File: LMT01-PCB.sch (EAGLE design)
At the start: 14 parts, among them IC3 PIC16F1826/27SO, IC4 MAX3467CPA, IC6 MCP23017SO

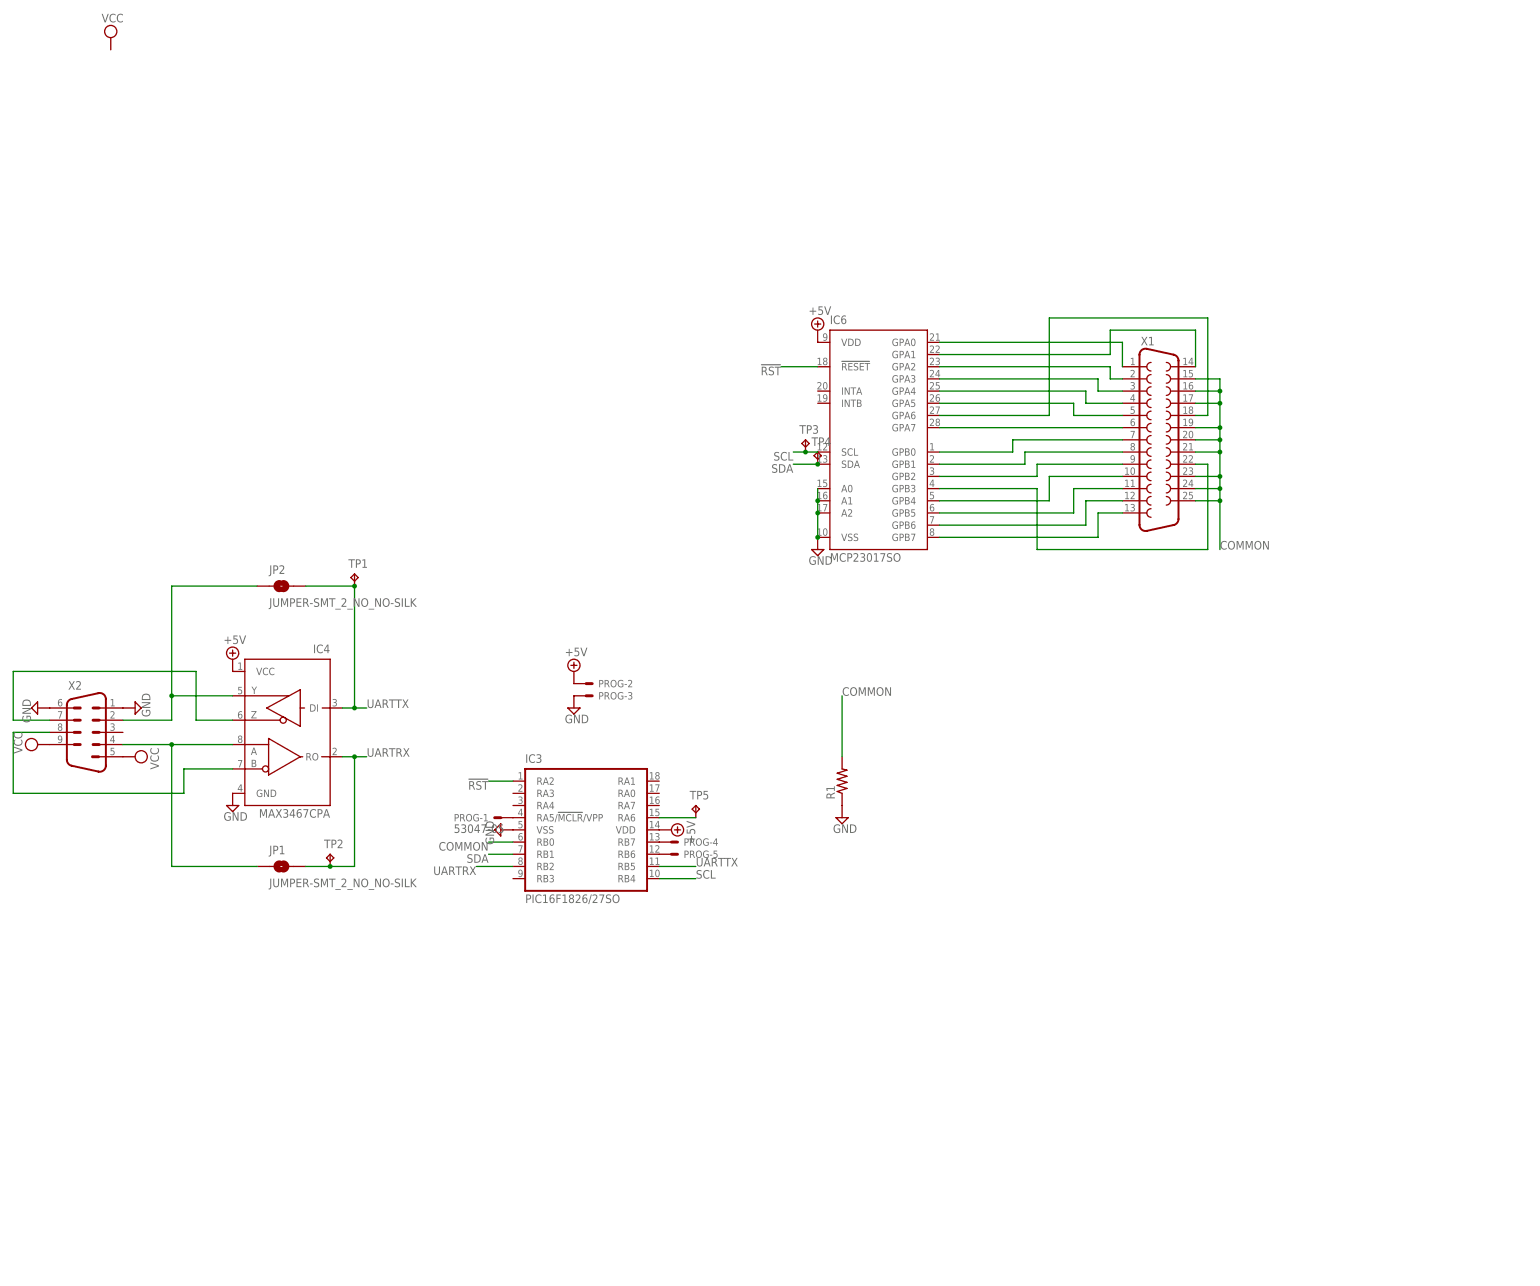
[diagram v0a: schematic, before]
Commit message: Switching to big PIC
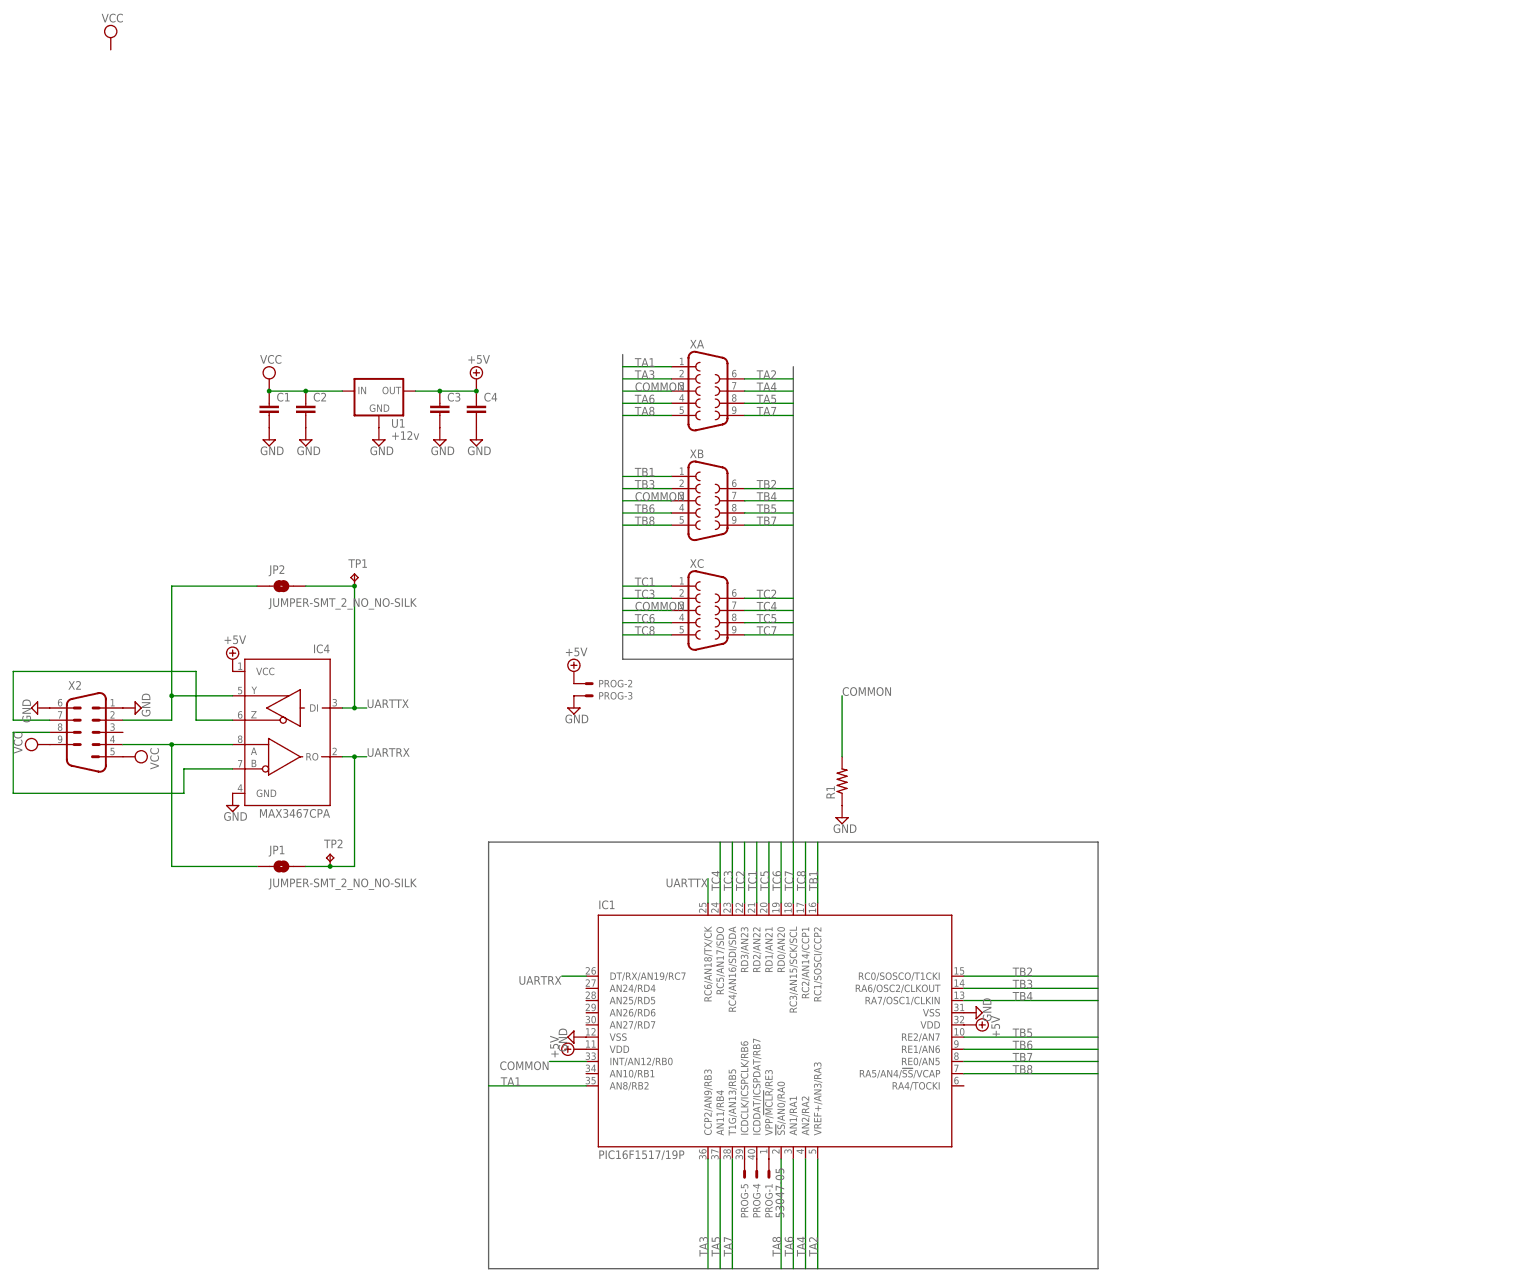
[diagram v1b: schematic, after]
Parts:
- removed IC3: PIC16F1826/27SO, microchip:PIC16F1826/27SO
- removed IC6: MCP23017SO, microchip:MCP23017SO
- removed TP3, TP4, TP5: TPB1,27, testpad:TPB1,27
- removed X1: (no value), con-subd:F25HP
- added C1, C2, C3, C4: (no value), resistor:C-EUC1206
- added IC1: PIC16F1517/19P, microchip:PIC16F1517/19P
- added U1: +12v, SparkFun-IC-Power:V_REG_78XX7812
- added XA, XB, XC: (no value), con-subd:F09HP
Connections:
- removed net !RST: IC3.RA2, IC6.!RESET
- removed net N$10: IC6.GPA5, X1.5
- removed net N$11: IC6.GPA6, X1.18
- removed net N$12: IC6.GPA7, X1.6
- removed net N$13: IC6.GPB0, X1.7
- removed net N$14: IC6.GPB1, X1.8
- removed net N$15: IC6.GPB2, X1.9
- removed net N$16: IC6.GPB3, X1.22
- removed net N$17: IC6.GPB4, X1.10
- removed net N$18: IC6.GPB5, X1.11
- removed net N$19: IC6.GPB6, X1.12
- removed net N$20: IC6.GPB7, X1.13
- removed net N$25: IC3.RB7, PROG-4.S
- removed net N$26: IC3.RB6, PROG-5.S
- removed net N$5: IC6.GPA0, X1.1
- removed net N$6: IC6.GPA1, X1.14
- removed net N$7: IC6.GPA2, X1.2
- removed net N$8: IC6.GPA3, X1.3
- removed net N$9: IC6.GPA4, X1.4
- removed net SCL: IC3.RB4, IC6.SCL, TP3.TP
- removed net SDA: IC3.RB1, IC6.SDA, TP4.TP
- new net N$2: IC1.ICDDAT/ICSPDAT/RB7, PROG-4.S
- new net TA1: IC1.AN8/RB2, XA.1
- new net TA2: IC1.VREF+/AN3/RA3, XA.6
- new net TA3: IC1.CCP2/AN9/RB3, XA.2
- new net TA4: IC1.AN2/RA2, XA.7
- new net TA5: IC1.AN11/RB4, XA.8
- new net TA6: IC1.AN1/RA1, XA.4
- new net TA7: IC1.T1G/AN13/RB5, XA.9
- new net TA8: IC1.!SS!/AN0/RA0, XA.5
- new net TB1: IC1.RC1/SOSCI/CCP2, XB.1
- new net TB2: IC1.RC0/SOSCO/T1CKI, XB.6
- new net TB3: IC1.RA6/OSC2/CLKOUT, XB.2
- new net TB4: IC1.RA7/OSC1/CLKIN, XB.7
- new net TB5: IC1.RE2/AN7, XB.8
- new net TB6: IC1.RE1/AN6, XB.4
- new net TB7: IC1.RE0/AN5, XB.9
- new net TB8: IC1.RA5/AN4/!SS!/VCAP, XB.5
- new net TC1: IC1.RD2/AN22, XC.1
- new net TC2: IC1.RD3/AN23, XC.6
- new net TC3: IC1.RC4/AN16/SDI/SDA, XC.2
- new net TC4: IC1.RC5/AN17/SDO, XC.7
- new net TC5: IC1.RD1/AN21, XC.8
- new net TC6: IC1.RD0/AN20, XC.4
- new net TC7: IC1.RC3/AN15/SCK/SCL, XC.9
- new net TC8: IC1.RC2/AN14/CCP1, XC.5
- net +5V: now also C3.1, C4.1, IC1.VDD, IC1.VDD@1, U1.OUT; no longer IC3.VDD, IC6.VDD
- net COMMON: now also IC1.INT/AN12/RB0, XA.3, XB.3, XC.3; no longer IC3.RB0, X1.15, X1.16, X1.17, X1.19, X1.20, X1.21, X1.23, X1.24, X1.25
- net GND: now also C1.2, C2.2, C3.2, C4.2, IC1.VSS, IC1.VSS@1, U1.GND; no longer IC3.VSS, IC6.A0, IC6.A1, IC6.A2, IC6.VSS
- net N$1: now also IC1.VPP/!MCLR!/RE3, PROG-1.S; no longer IC3.RA6, TP5.TP
- net N$3: now also IC1.ICDCLK/ICSPCLK/RB6, PROG-5.S; no longer IC3.RA5/!MCLR!/VPP, PROG-1.S
- net UARTRX: now also IC1.DT/RX/AN19/RC7; no longer IC3.RB2
- net UARTTX: now also IC1.RC6/AN18/TX/CK; no longer IC3.RB5
- net VCC: now also C1.1, C2.1, U1.IN
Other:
- moved on the sheet: PROG-1, PROG-4, PROG-5

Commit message: PIC18
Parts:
- added C5, C6: (no value), resistor:C-EUC1206
- added R2, R3: (no value), resistor:R-US_R1206
- IC1: value PIC16F1517/19P -> PIC18F47K40; device microchip:PIC16F1517/19P -> microchip:PIC18F47K40
- renumbered U1 to IC2
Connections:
- removed net COMMON: IC1.INT/AN12/RB0, R1.2, XA.3, XB.3, XC.3
- new net COMMONA: IC1.RB3, R1.2, XA.3
- new net COMMONB: IC1.RC0, R2.2, XB.3
- new net COMMONC: IC1.RC6, R3.2, XC.3
- net +5V: now also C5.1, C6.1, IC1.VDD@2; no longer IC1.VDD
- net GND: now also C5.2, C6.2, IC1.VSS@2, R2.1, R3.1; no longer IC1.VSS
- net N$1: now also IC1.RE3; no longer IC1.VPP/!MCLR!/RE3
- net N$2: now also IC1.RB7; no longer IC1.ICDDAT/ICSPDAT/RB7
- net N$3: now also IC1.RB6; no longer IC1.ICDCLK/ICSPCLK/RB6
- net TA1: now also IC1.RB1; no longer IC1.AN8/RB2
- net TA2: now also IC1.RA3; no longer IC1.VREF+/AN3/RA3
- net TA3: now also IC1.RB2; no longer IC1.CCP2/AN9/RB3
- net TA4: now also IC1.RA2; no longer IC1.AN2/RA2
- net TA5: now also IC1.RB4; no longer IC1.AN11/RB4
- net TA6: now also IC1.RA1; no longer IC1.AN1/RA1
- net TA7: now also IC1.RB5; no longer IC1.T1G/AN13/RB5
- net TA8: now also IC1.RA0; no longer IC1.!SS!/AN0/RA0
- net TB1: now also IC1.RD4; no longer IC1.RC1/SOSCI/CCP2
- net TB2: now also IC1.RA6; no longer IC1.RC0/SOSCO/T1CKI
- net TB3: now also IC1.RD5; no longer IC1.RA6/OSC2/CLKOUT
- net TB4: now also IC1.RA7; no longer IC1.RA7/OSC1/CLKIN
- net TB5: now also IC1.RD6; no longer IC1.RE2/AN7
- net TB6: now also IC1.RD7; no longer IC1.RE1/AN6
- net TB7: now also IC1.RE2; no longer IC1.RE0/AN5
- net TB8: now also IC1.RE1; no longer IC1.RA5/AN4/!SS!/VCAP
- net TC1: now also IC1.RD2; no longer IC1.RD2/AN22
- net TC2: now also IC1.RD3; no longer IC1.RD3/AN23
- net TC3: now also IC1.RC4; no longer IC1.RC4/AN16/SDI/SDA
- net TC4: now also IC1.RC5; no longer IC1.RC5/AN17/SDO
- net TC5: now also IC1.RD1; no longer IC1.RD1/AN21
- net TC6: now also IC1.RD0; no longer IC1.RD0/AN20
- net TC7: now also IC1.RC3; no longer IC1.RC3/AN15/SCK/SCL
- net TC8: now also IC1.RC2; no longer IC1.RC2/AN14/CCP1
- net UARTRX: now also IC1.RC7; no longer IC1.DT/RX/AN19/RC7
- net UARTTX: now also IC1.RB0; no longer IC1.RC6/AN18/TX/CK
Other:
- moved on the sheet: PROG-1, PROG-4, PROG-5

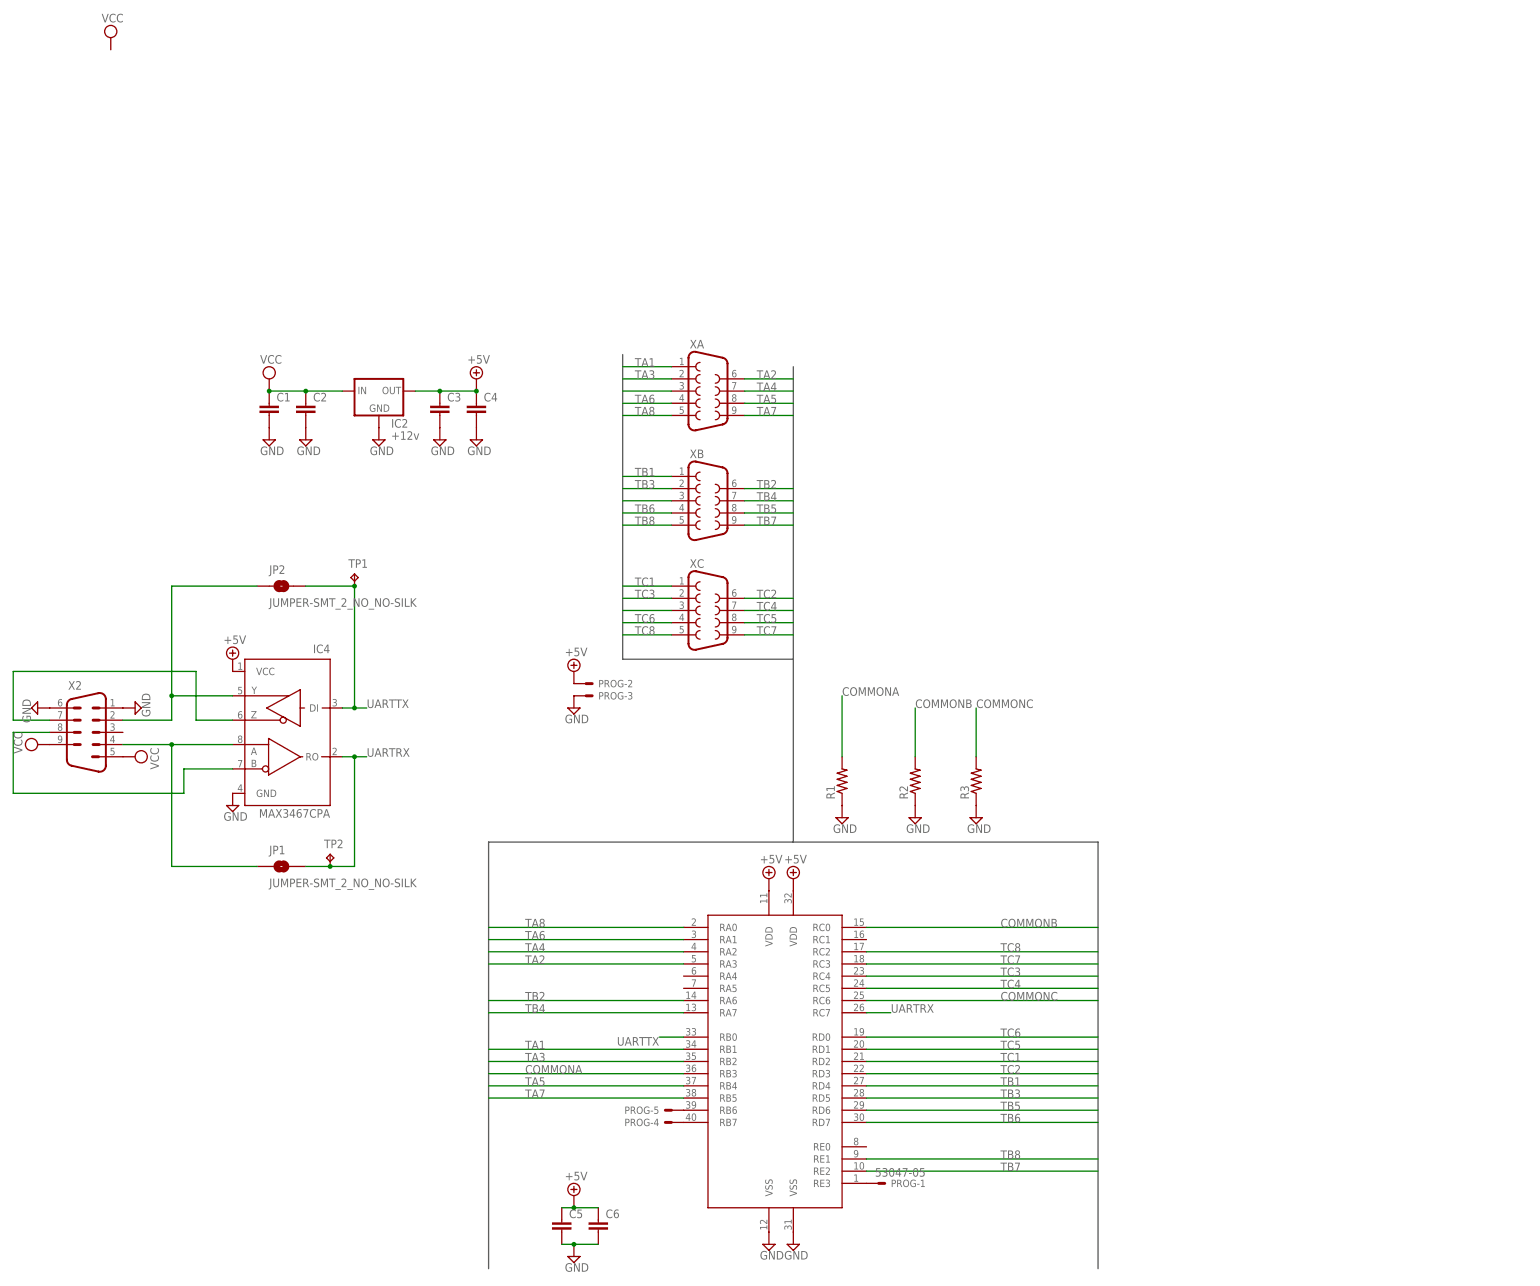
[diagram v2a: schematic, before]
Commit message: Adding optional comparators and voltage reference
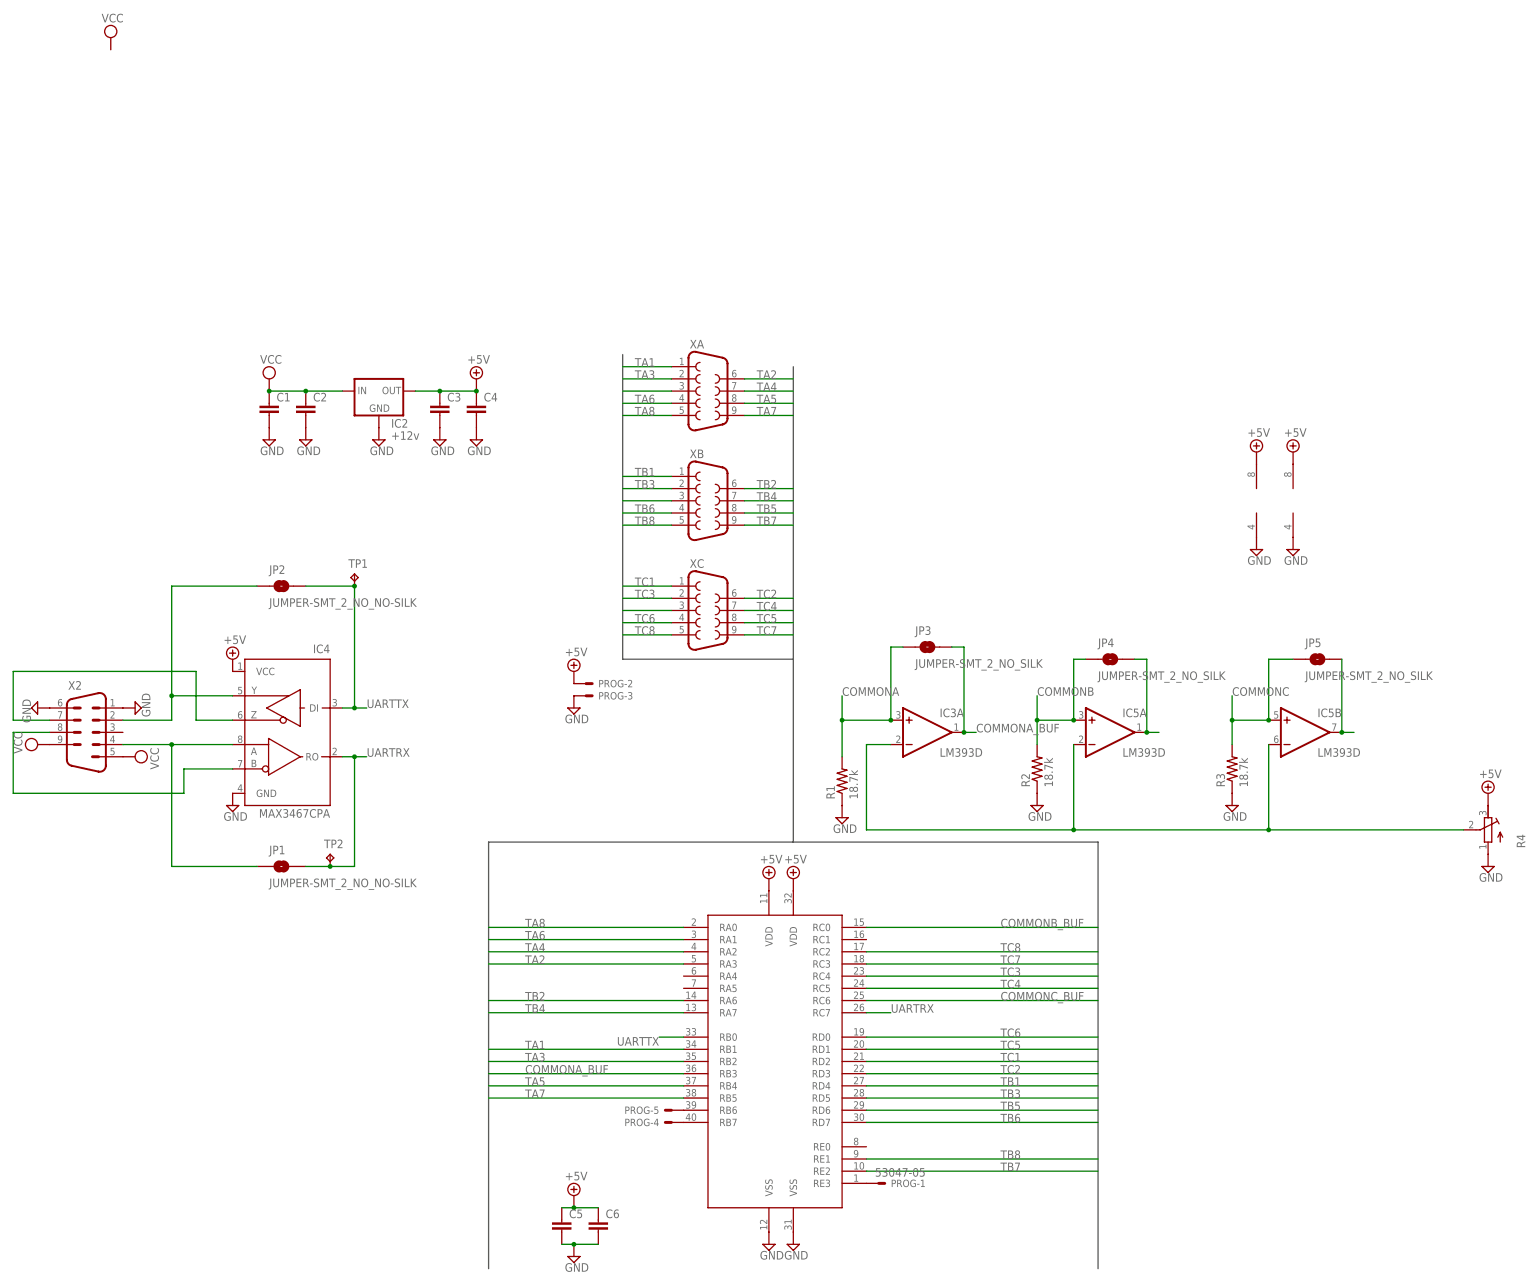
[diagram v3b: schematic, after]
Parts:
- added IC3, IC5: LM393D, linear:LM393D
- added JP3, JP4, JP5: JUMPER-SMT_2_NO_SILK, SparkFun-Jumpers:JUMPER-SMT_2_NO_SILK
- added R4: (no value), resistor:R-TRIMM4G/J
- R1, R2, R3: value (none) -> 18.7k
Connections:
- new net COMMONA_BUF: IC1.RB3, IC3A.OUT, JP3.2
- new net COMMONB_BUF: IC1.RC0, IC5A.OUT, JP4.2
- new net COMMONC_BUF: IC1.RC6, IC5B.OUT, JP5.2
- new net N$4: IC3A.-IN, IC5A.-IN, IC5B.-IN, R4.S
- net +5V: now also IC3P.V+, IC5P.V+, R4.E
- net COMMONA: now also IC3A.+IN, JP3.1; no longer IC1.RB3
- net COMMONB: now also IC5A.+IN, JP4.1; no longer IC1.RC0
- net COMMONC: now also IC5B.+IN, JP5.1; no longer IC1.RC6
- net GND: now also IC3P.V-, IC5P.V-, R4.A
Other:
- moved on the sheet: R2, R3
